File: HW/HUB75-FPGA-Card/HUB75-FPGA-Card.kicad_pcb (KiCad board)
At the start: 4 copper layers, 53.3 x 85.7 mm, 24 parts, among them J1 Conn_02x08_Odd_Even, J2 Conn_02x08_Odd_Even, U1 T20Q100F3, U2 74AHCT245PW, U3 74AHCT245PW, U4 74AHCT245PW, U6 FT232H, U7 93LCxxBxxOT

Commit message: add usb audio implementation
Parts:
- moved U1 14.0 mm to (115.6, 79.4), turned to 45 degrees

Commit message: finish up schematic and begin routing
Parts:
- added C1: 100n, Capacitor_SMD:C_0603_1608Metric, F.Cu at (128.0, 85.3)
- added C10: 1u, Capacitor_SMD:C_0603_1608Metric, F.Cu at (130.6, 90.4)
- added C11: 1u, Capacitor_SMD:C_0603_1608Metric, F.Cu at (124.5, 90.4)
- added C12: 100n, Capacitor_SMD:C_0603_1608Metric, F.Cu at (119.6, 92.2)
- added C13: 4.7u, Capacitor_SMD:C_0603_1608Metric, F.Cu at (121.2, 92.2)
- added C14: 100n, Capacitor_SMD:C_0603_1608Metric, F.Cu at (121.7, 72.9)
- added C15: 100n, Capacitor_SMD:C_0603_1608Metric, F.Cu at (124.7, 78.5)
- added C16: 100n, Capacitor_SMD:C_0603_1608Metric, F.Cu at (124.7, 82.8)
- added C17: 100n, Capacitor_SMD:C_0603_1608Metric, F.Cu at (112.8, 92.2)
- added C18: 100n, Capacitor_SMD:C_0603_1608Metric, F.Cu at (116.6, 92.2)
- added C2: 4.7u, Capacitor_SMD:C_0603_1608Metric, F.Cu at (113.6, 85.6)
- added C20: 100n, Capacitor_SMD:C_0603_1608Metric, F.Cu at (103.9, 81.3)
- added C21: 100n, Capacitor_SMD:C_0603_1608Metric, F.Cu at (103.9, 84.3)
- added C22: 100n, Capacitor_SMD:C_0603_1608Metric, F.Cu at (109.7, 71.6)
- added C23: 1u, Capacitor_SMD:C_0603_1608Metric, F.Cu at (101.4, 77.0)
- added C24: 1u, Capacitor_SMD:C_0603_1608Metric, F.Cu at (101.4, 70.9)
- added C25: 100n, Capacitor_SMD:C_0603_1608Metric, F.Cu at (99.7, 62.9)
- added C26: 100n, Capacitor_SMD:C_0603_1608Metric, F.Cu at (109.9, 62.9)
- added C27: 100n, Capacitor_SMD:C_0603_1608Metric, F.Cu at (120.0, 62.9)
- added C3: 10u, Capacitor_SMD:C_0603_1608Metric, F.Cu at (103.9, 82.8)
- added C36: 100n, Capacitor_SMD:C_0603_1608Metric, F.Cu at (122.9, 141.1)
- added C37: 4.7u, Capacitor_SMD:C_0603_1608Metric, F.Cu at (122.2, 135.5)
- added C38: 100n, Capacitor_SMD:C_0603_1608Metric, F.Cu at (122.2, 138.0)
- added C39: 4.7u, Capacitor_SMD:C_0603_1608Metric, F.Cu at (122.2, 146.2)
- added C4: 1u, Capacitor_SMD:C_0603_1608Metric, F.Cu at (109.2, 93.0)
- added C40: 4.7u, Capacitor_SMD:C_0603_1608Metric, F.Cu at (127.5, 142.3)
- added C41: 100n, Capacitor_SMD:C_0603_1608Metric, F.Cu at (127.5, 144.8)
- added C42: 4.7u, Capacitor_SMD:C_0603_1608Metric, F.Cu at (142.1, 149.3)
- added C43: 100n, Capacitor_SMD:C_0603_1608Metric, F.Cu at (145.0, 149.3)
- added C44: 100n, Capacitor_SMD:C_0603_1608Metric, F.Cu at (147.5, 149.3)
- added C45: 100n, Capacitor_SMD:C_0603_1608Metric, F.Cu at (150.0, 149.3)
- added C46: 100n, Capacitor_SMD:C_0603_1608Metric, F.Cu at (124.2, 152.2)
- added C47: 1u, Capacitor_SMD:C_0603_1608Metric, F.Cu at (118.7, 152.2)
- added C48: 1u, Capacitor_SMD:C_0603_1608Metric, F.Cu at (147.5, 136.6)
- added C49: 1u, Capacitor_SMD:C_0603_1608Metric, F.Cu at (150.0, 136.6)
- added C5: 100n, Capacitor_SMD:C_0603_1608Metric, F.Cu at (118.1, 92.2)
- added C50: 1u, Capacitor_SMD:C_0603_1608Metric, F.Cu at (151.0, 145.7)
- added C51: 1u, Capacitor_SMD:C_0603_1608Metric, F.Cu at (121.7, 99.3)
- added C52: 10u, Capacitor_SMD:C_0603_1608Metric, F.Cu at (120.1, 99.3)
- added C53: 100n, Capacitor_SMD:C_0603_1608Metric, F.Cu at (118.6, 99.3)
- added C54: 100n, Capacitor_SMD:C_0603_1608Metric, F.Cu at (129.3, 99.8)
- added C55: 10u, Capacitor_SMD:C_0603_1608Metric, F.Cu at (107.2, 112.8)
- added C6: 100n, Capacitor_SMD:C_0603_1608Metric, F.Cu at (124.7, 80.5)
- added C7: 100n, Capacitor_SMD:C_0603_1608Metric, F.Cu at (123.2, 72.9)
- added C8: 100n, Capacitor_SMD:C_0603_1608Metric, F.Cu at (117.3, 71.6)
- added C9: 100n, Capacitor_SMD:C_0603_1608Metric, F.Cu at (113.0, 71.6)
- added D1: LED, Diode_SMD:D_0603_1608Metric, F.Cu at (107.5, 148.2)
- added FB3: FerriteBead_Small, Resistor_SMD:R_0603_1608Metric, F.Cu at (102.9, 101.6)
- added FB4: FerriteBead_Small, Resistor_SMD:R_0603_1608Metric, F.Cu at (118.9, 136.3)
- added FB5: FerriteBead_Small, Resistor_SMD:R_0603_1608Metric, F.Cu at (124.2, 143.7)
- added H1: MountingHole, MountingHole:MountingHole_3.2mm_M3, F.Cu at (91.4, 51.4)
- added H2: MountingHole, MountingHole:MountingHole_3.2mm_M3, F.Cu at (91.4, 128.9)
- added H3: MountingHole, MountingHole:MountingHole_3.2mm_M3, F.Cu at (137.2, 51.4)
- added H4: MountingHole, MountingHole:MountingHole_3.2mm_M3, F.Cu at (137.2, 128.9)
- added J1: Conn_02x04_Odd_Even, Connector_PinHeader_2.54mm:PinHeader_2x04_P2.54mm_Vertical, F.Cu at (89.9, 99.8)
- added J10: USB_A_Stacked, Connector_USB:USB_A_CUI_UJ2-ADH-TH_Horizontal_Stacked, F.Cu at (100.9, 114.9)
- added J11: Conn_01x01, Connector_Wire:SolderWire-2sqmm_1x01_D2mm_OD3.9mm, F.Cu at (98.4, 51.4)
- added J12: Conn_01x01, Connector_Wire:SolderWire-2sqmm_1x01_D2mm_OD3.9mm, F.Cu at (130.2, 51.4)
- added J2: Conn_01x03, Connector_PinHeader_2.54mm:PinHeader_1x03_P2.54mm_Vertical, F.Cu at (104.8, 50.8)
- added J4: Conn_01x03, Connector_PinHeader_2.54mm:PinHeader_1x03_P2.54mm_Vertical, F.Cu at (111.1, 50.8)
- added J5: Conn_01x03, Connector_PinHeader_2.54mm:PinHeader_1x03_P2.54mm_Vertical, F.Cu at (117.5, 50.8)
- added J7: Conn_01x03, Connector_PinHeader_2.54mm:PinHeader_1x03_P2.54mm_Vertical, F.Cu at (123.8, 50.8)
- added J8: Conn_01x04, TerminalBlock_Phoenix:TerminalBlock_Phoenix_PT-1,5-4-5.0-H_1x04_P5.00mm_Horizontal, F.Cu at (135.3, 122.4)
- added J9: USB_C_Receptacle_USB2.0, Connector_USB:USB_C_Receptacle_GCT_USB4105-xx-A_16P_TopMnt_Horizontal, F.Cu at (137.2, 97.8)
- added R1: 10k, Resistor_SMD:R_0603_1608Metric, F.Cu at (103.9, 87.4)
- added R10: 10k, Resistor_SMD:R_0603_1608Metric, F.Cu at (110.5, 85.6)
- added R11: 10k, Resistor_SMD:R_0603_1608Metric, F.Cu at (110.5, 87.4)
- added R18: 68R, Resistor_SMD:R_0603_1608Metric, F.Cu at (107.4, 146.5)
- added R19: 10k, Resistor_SMD:R_0603_1608Metric, F.Cu at (108.2, 142.9)
- added R2: 10k, Resistor_SMD:R_0603_1608Metric, F.Cu at (118.6, 81.5)
- added R20: 5.1k, Resistor_SMD:R_0603_1608Metric, F.Cu at (130.8, 102.4)
- added R21: 5.1k, Resistor_SMD:R_0603_1608Metric, F.Cu at (130.8, 93.2)
- added R3: 10k, Resistor_SMD:R_0603_1608Metric, F.Cu at (118.6, 83.3)
- added R4: 10k, Resistor_SMD:R_0603_1608Metric, F.Cu at (118.4, 84.8)
- added R5: 10k, Resistor_SMD:R_0603_1608Metric, F.Cu at (118.6, 86.6)
- added R6: 10k, Resistor_SMD:R_0603_1608Metric, F.Cu at (113.5, 87.4)
- added R7: 10k, Resistor_SMD:R_0603_1608Metric, F.Cu at (103.9, 85.9)
- added R8: 10k, Resistor_SMD:R_0603_1608Metric, F.Cu at (110.5, 84.1)
- added R9: 10k, Resistor_SMD:R_0603_1608Metric, F.Cu at (110.5, 82.5)
- added U10: HS-100B, Package_QFP:LQFP-48_7x7mm_P0.5mm, F.Cu at (115.3, 143.4)
- added U11: PAM8406, Package_SO:SO-16_3.9x9.9mm_P1.27mm, F.Cu at (144.7, 142.5)
- added U12: USBLC6-2SC6, Package_TO_SOT_SMD:SOT-23-6, F.Cu at (128.5, 97.3)
- added U13: CH334R, Package_SO:SSOP-16_3.9x4.9mm_P0.635mm, F.Cu at (122.2, 104.7)
- added U2: XC6206PxxxMR, Package_TO_SOT_SMD:SOT-23-3, F.Cu at (127.5, 90.4)
- added U3: AP2112K-1.2, Package_TO_SOT_SMD:SOT-23-5, F.Cu at (101.4, 73.9)
- added U9: WMM7037AT2, Project:WMM7037AT2, F.Cu at (121.4, 151.6)
- added X1: ECS-2520MV-xxx-xx, Oscillator:Oscillator_SMD_ECS_2520MV-xxx-xx-4Pin_2.5x2.0mm, F.Cu at (125.5, 85.3)
- added Y1: Crystal_GND24, Crystal:Crystal_SMD_3225-4Pin_3.2x2.5mm, F.Cu at (117.6, 103.4)
- C28: renamed from C10; footprint Capacitor_SMD:C_0603_1608Metric_Pad1.08x0.95mm_HandSolder -> Capacitor_SMD:C_0603_1608Metric
- C29: renamed from C11; footprint Capacitor_SMD:C_0603_1608Metric_Pad1.08x0.95mm_HandSolder -> Capacitor_SMD:C_0603_1608Metric
- C30: renamed from C12; footprint Capacitor_SMD:C_0603_1608Metric_Pad1.08x0.95mm_HandSolder -> Capacitor_SMD:C_0603_1608Metric
- C31: renamed from C13; footprint Capacitor_SMD:C_0603_1608Metric_Pad1.08x0.95mm_HandSolder -> Capacitor_SMD:C_0603_1608Metric
- C32: renamed from C14; footprint Capacitor_SMD:C_0603_1608Metric_Pad1.08x0.95mm_HandSolder -> Capacitor_SMD:C_0603_1608Metric
- C33: renamed from C6; footprint Capacitor_SMD:C_0603_1608Metric_Pad1.08x0.95mm_HandSolder -> Capacitor_SMD:C_0603_1608Metric
- C34: renamed from C8; footprint Capacitor_SMD:C_0603_1608Metric_Pad1.08x0.95mm_HandSolder -> Capacitor_SMD:C_0603_1608Metric
- C35: renamed from C5; footprint Capacitor_SMD:C_0603_1608Metric_Pad1.08x0.95mm_HandSolder -> Capacitor_SMD:C_0603_1608Metric
- FB1, FB2: value FerriteBead -> FerriteBead_Small; footprint Resistor_SMD:R_0603_1608Metric_Pad0.98x0.95mm_HandSolder -> Resistor_SMD:R_0603_1608Metric
- R12: renamed from R15; footprint Resistor_SMD:R_0603_1608Metric_Pad0.98x0.95mm_HandSolder -> Resistor_SMD:R_0603_1608Metric
- R13: renamed from R11; footprint Resistor_SMD:R_0603_1608Metric_Pad0.98x0.95mm_HandSolder -> Resistor_SMD:R_0603_1608Metric
- R14: renamed from R12; footprint Resistor_SMD:R_0603_1608Metric_Pad0.98x0.95mm_HandSolder -> Resistor_SMD:R_0603_1608Metric
- R15: renamed from R14; footprint Resistor_SMD:R_0603_1608Metric_Pad0.98x0.95mm_HandSolder -> Resistor_SMD:R_0603_1608Metric
- R16: footprint Resistor_SMD:R_0603_1608Metric_Pad0.98x0.95mm_HandSolder -> Resistor_SMD:R_0603_1608Metric
- R17: renamed from R13; footprint Resistor_SMD:R_0603_1608Metric_Pad0.98x0.95mm_HandSolder -> Resistor_SMD:R_0603_1608Metric
- moved U7 73.5 mm to (99.8, 94.7), turned to 90 degrees
- moved C32 67.9 mm to (93.0, 97.0), turned to 180 degrees
- moved R12 67.7 mm to (98.8, 87.9), turned to 90 degrees
- moved R16 67.0 mm to (98.3, 101.6), turned to -90 degrees
- moved FB2 65.7 mm to (95.2, 101.6), turned to 90 degrees
- moved C34 64.2 mm to (93.0, 91.7), turned to 180 degrees
- moved C33 63.8 mm to (93.0, 93.2), turned to 180 degrees
- moved U8 61.0 mm to (109.2, 102.9)
- moved C28 59.8 mm to (96.8, 101.6), turned to -90 degrees
- moved R17 59.5 mm to (106.2, 102.9), turned to 90 degrees
- moved R15 56.0 mm to (109.7, 105.4), turned to 180 degrees
- moved C31 55.7 mm to (105.4, 90.7)
- moved C29 55.4 mm to (101.3, 101.6), turned to -90 degrees
- moved C30 52.6 mm to (104.6, 99.3)
- moved R13 49.1 mm to (112.0, 101.3), turned to -90 degrees
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- renumbered J1 to J3, J2 to J6, U2 to U4, U3 to U5, U4 to U6, U6 to U7, U7 to U8
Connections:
- C28 pad 1: Net-(U6-VPHY) -> Net-(U7-VPHY)
- C29 pad 1: Net-(U6-VPLL) -> Net-(U7-VPLL)
- FB1 pad 1: +3.3VP -> +1V2
- FB1 pad 2: Net-(U6-VPHY) -> Net-(U1A-VCCA_BR)
- FB2 pad 2: Net-(U6-VPLL) -> Net-(U7-VPHY)
- J3 pad 1: /Hub75/B1 -> /Level Shifters/B1_out
- J3 pad 11: unconnected-(J1-Pin_11-Pad11) -> /Level Shifters/RDAT_out
- J3 pad 13: unconnected-(J1-Pin_13-Pad13) -> /Level Shifters/CLK_out
- J3 pad 14: unconnected-(J1-Pin_14-Pad14) -> /Level Shifters/LAT_out
- J3 pad 15: unconnected-(J1-Pin_15-Pad15) -> /Level Shifters/BLNK_out
- J3 pad 2: /Hub75/G1 -> /Level Shifters/G1_out
- J3 pad 3: /Hub75/R1 -> /Level Shifters/R1_out
- J3 pad 5: /Hub75/B2 -> /Level Shifters/B2_out
- J3 pad 6: /Hub75/G2 -> /Level Shifters/G2_out
- J3 pad 7: /Hub75/R2 -> /Level Shifters/R2_out
- J3 pad 9: unconnected-(J1-Pin_9-Pad9) -> /Level Shifters/RCLK_out
- J6 pad 1: /Hub75/B3 -> /Level Shifters/B3_out
- J6 pad 11: unconnected-(J2-Pin_11-Pad11) -> /Level Shifters/RDAT_out
- J6 pad 13: unconnected-(J2-Pin_13-Pad13) -> /Level Shifters/CLK_out
- J6 pad 14: unconnected-(J2-Pin_14-Pad14) -> /Level Shifters/LAT_out
- J6 pad 15: unconnected-(J2-Pin_15-Pad15) -> /Level Shifters/BLNK_out
- J6 pad 2: /Hub75/G3 -> /Level Shifters/G3_out
- J6 pad 3: /Hub75/R3 -> /Level Shifters/R3_out
- J6 pad 5: /Hub75/B4 -> /Level Shifters/B4_out
- J6 pad 6: /Hub75/G4 -> /Level Shifters/G4_out
- J6 pad 7: /Hub75/R4 -> /Level Shifters/R4_out
- J6 pad 9: unconnected-(J2-Pin_9-Pad9) -> /Level Shifters/RCLK_out
- U1 pad 10: unconnected-(U1B-GPIOL_20_CTRL0_CDI4-Pad10) -> /FPGA/~{TXE}
- U1 pad 100: unconnected-(U1B-GPIOL_46-Pad100) -> /FPGA/B2
- U1 pad 11: unconnected-(U1A-VCCIO1A_1B_1C-Pad11) -> +3V3
- U1 pad 12: unconnected-(U1B-TDO-Pad12) -> /FPGA/TDO
- U1 pad 13: unconnected-(U1B-TCK-Pad13) -> Net-(J1-Pin_3)
- U1 pad 14: unconnected-(U1B-GPIOL_13_CDI3-Pad14) -> /FPGA/CLK_12MHZ
- U1 pad 15: unconnected-(U1A-VCC-Pad15) -> +1V2
- U1 pad 16: unconnected-(U1B-TMS-Pad16) -> /FPGA/TMS
- U1 pad 17: unconnected-(U1B-TDI-Pad17) -> /FPGA/TDI
- U1 pad 2: unconnected-(U1B-GPIOL_41_CDI9-Pad2) -> /FPGA/B1
- U1 pad 20: unconnected-(U1B-CRESET_N-Pad20) -> /FPGA/CRESET_N
- U1 pad 21: unconnected-(U1A-VCCIO1A_1B_1C-Pad21) -> +3V3
- U1 pad 22: unconnected-(U1B-GPIOL_05_CSO-Pad22) -> /FPGA/~{RXF}
- U1 pad 29: unconnected-(U1D-GPIOB_TXP01-Pad29) -> /FPGA/D7
- U1 pad 3: unconnected-(U1B-GPIOL_40_CDI8-Pad3) -> /FPGA/G1
- U1 pad 30: unconnected-(U1D-GPIOB_TXN01-Pad30) -> /FPGA/D6
- U1 pad 31: unconnected-(U1A-VCC-Pad31) -> +1V2
- U1 pad 32: unconnected-(U1D-GPIOB_TXP04-Pad32) -> /FPGA/D5
- U1 pad 33: unconnected-(U1D-GPIOB_TXN04-Pad33) -> /FPGA/D4
- U1 pad 34: unconnected-(U1A-VCCIO4B-Pad34) -> +3V3
- U1 pad 37: unconnected-(U1D-GPIOB_TXP10-Pad37) -> /FPGA/D3
- U1 pad 38: unconnected-(U1D-GPIOB_TXN10-Pad38) -> /FPGA/D2
- U1 pad 4: unconnected-(U1B-GPIOL_32_CTRL4_CDI7-Pad4) -> /FPGA/R1
- U1 pad 40: unconnected-(U1D-GPIOB_RXP00-Pad40) -> /FPGA/D1
- U1 pad 41: unconnected-(U1D-GPIOB_RXN00-Pad41) -> /FPGA/D0
- U1 pad 42: unconnected-(U1A-VCCIO4A-Pad42) -> +3V3
- U1 pad 45: unconnected-(U1A-VCC-Pad45) -> +1V2
- U1 pad 5: unconnected-(U1B-GPIOL_31_CLK7_CDI6-Pad5) -> /FPGA/~{OE}
- U1 pad 50: unconnected-(U1A-VCCA_BR-Pad50) -> Net-(U1A-VCCA_BR)
- U1 pad 54: unconnected-(U1C-GPIOR_157_PLLIN-Pad54) -> Net-(U1C-GPIOR_157_PLLIN)
- U1 pad 60: unconnected-(U1A-VCCIO3D_3E-Pad60) -> +3V3
- U1 pad 64: unconnected-(U1A-VCC-Pad64) -> +1V2
- U1 pad 69: unconnected-(U1A-VCCIO3B_3C-Pad69) -> +3V3
- U1 pad 7: unconnected-(U1B-GPIOL_24_CLK0-Pad7) -> /FPGA/CLK_60MHZ
- U1 pad 72: unconnected-(U1A-VCCA_TR-Pad72) -> Net-(U1A-VCCA_BR)
- U1 pad 73: unconnected-(U1C-GPIOR_88_CDI28-Pad73) -> /FPGA/R3
- U1 pad 74: unconnected-(U1C-GPIOR_87_CDI29-Pad74) -> /FPGA/B3
- U1 pad 75: unconnected-(U1A-VCC-Pad75) -> +1V2
- U1 pad 76: unconnected-(U1A-VCCIO3A-Pad76) -> +3V3
- U1 pad 77: unconnected-(U1C-GPIOR_79_EXTFB1_CDI30-Pad77) -> /FPGA/G3
- U1 pad 78: unconnected-(U1C-GPIOR_78_EXTFB0_CDI31-Pad78) -> /FPGA/G4
- U1 pad 79: unconnected-(U1C-GPIOR_77_PLLIN1-Pad79) -> /FPGA/B4
- U1 pad 8: unconnected-(U1B-GPIOL_12_CDI2-Pad8) -> /FPGA/~{WR}
- U1 pad 80: unconnected-(U1C-GPIOR_76_PLLIN0-Pad80) -> /FPGA/R4
- U1 pad 82: unconnected-(U1A-VCC-Pad82) -> +1V2
- U1 pad 83: unconnected-(U1A-VCC-Pad83) -> +1V2
- U1 pad 84: unconnected-(U1A-VCCA_TL-Pad84) -> Net-(U1A-VCCA_BR)
- U1 pad 85: unconnected-(U1B-GPIOL_75_PLLIN1-Pad85) -> /FPGA/STRIP4
- U1 pad 86: unconnected-(U1B-GPIOL_74_PLLIN0-Pad86) -> /FPGA/STRIP3
- U1 pad 87: unconnected-(U1B-GPIOL_73_EXTFB1_CDI15-Pad87) -> /FPGA/BLANK
- U1 pad 88: unconnected-(U1B-GPIOL_71_NSTATUS-Pad88) -> /FPGA/LAT
- U1 pad 89: unconnected-(U1B-GPIOL_72_EXTFB0_CDI14-Pad89) -> /FPGA/CLKOUT
- U1 pad 9: unconnected-(U1B-GPIOL_21_CTRL1_CDI5-Pad9) -> /FPGA/~{RD}
- U1 pad 91: unconnected-(U1A-VCC-Pad91) -> +1V2
- U1 pad 92: unconnected-(U1B-GPIOL_70_CBSEL0-Pad92) -> /FPGA/ROW_DATA
- U1 pad 93: unconnected-(U1B-GPIOL_69_CBSEL1-Pad93) -> /FPGA/ROW_CLK
- U1 pad 94: unconnected-(U1B-GPIOL_67_CDI13-Pad94) -> /FPGA/STRIP2
- U1 pad 95: unconnected-(U1B-GPIOL_66_CDI12-Pad95) -> /FPGA/STRIP1
- U1 pad 96: unconnected-(U1A-VCCIO1D_1E-Pad96) -> +3V3
- U1 pad 98: unconnected-(U1B-GPIOL_53_CDI10-Pad98) -> /FPGA/R2
- U1 pad 99: unconnected-(U1B-GPIOL_54_CDI11-Pad99) -> /FPGA/G2
- U4 pad 1: unconnected-(U2-A->B-Pad1) -> +5V
- U4 pad 11: unconnected-(U2-B7-Pad11) -> /Level Shifters/LED2_out
- U4 pad 12: unconnected-(U2-B6-Pad12) -> /Level Shifters/LED1_out
- U4 pad 13: unconnected-(U2-B5-Pad13) -> /Level Shifters/R2_out
- U4 pad 14: unconnected-(U2-B4-Pad14) -> /Level Shifters/G2_out
- U4 pad 15: unconnected-(U2-B3-Pad15) -> /Level Shifters/B2_out
- U4 pad 16: unconnected-(U2-B2-Pad16) -> /Level Shifters/B1_out
- U4 pad 17: unconnected-(U2-B1-Pad17) -> /Level Shifters/G1_out
- U4 pad 18: unconnected-(U2-B0-Pad18) -> /Level Shifters/R1_out
- U4 pad 2: unconnected-(U2-A0-Pad2) -> /FPGA/R1
- U4 pad 3: unconnected-(U2-A1-Pad3) -> /FPGA/G1
- U4 pad 4: unconnected-(U2-A2-Pad4) -> /FPGA/B1
- U4 pad 5: unconnected-(U2-A3-Pad5) -> /FPGA/B2
- U4 pad 6: unconnected-(U2-A4-Pad6) -> /FPGA/G2
- U4 pad 7: unconnected-(U2-A5-Pad7) -> /FPGA/R2
- U4 pad 8: unconnected-(U2-A6-Pad8) -> /FPGA/STRIP1
- U4 pad 9: unconnected-(U2-A7-Pad9) -> /FPGA/STRIP2
- U5 pad 1: unconnected-(U3-A->B-Pad1) -> +5V
- U5 pad 14: unconnected-(U3-B4-Pad14) -> /Level Shifters/BLNK_out
- U5 pad 15: unconnected-(U3-B3-Pad15) -> /Level Shifters/LAT_out
- U5 pad 16: unconnected-(U3-B2-Pad16) -> /Level Shifters/CLK_out
- U5 pad 17: unconnected-(U3-B1-Pad17) -> /Level Shifters/RDAT_out
- U5 pad 18: unconnected-(U3-B0-Pad18) -> /Level Shifters/RCLK_out
- U5 pad 2: unconnected-(U3-A0-Pad2) -> /FPGA/ROW_CLK
- U5 pad 3: unconnected-(U3-A1-Pad3) -> /FPGA/ROW_DATA
- U5 pad 4: unconnected-(U3-A2-Pad4) -> /FPGA/CLKOUT
- U5 pad 5: unconnected-(U3-A3-Pad5) -> /FPGA/LAT
- U5 pad 6: unconnected-(U3-A4-Pad6) -> /FPGA/BLANK
- U5 pad 7: unconnected-(U3-A5-Pad7) -> GND
- U5 pad 8: unconnected-(U3-A6-Pad8) -> GND
- U5 pad 9: unconnected-(U3-A7-Pad9) -> GND
- U6 pad 1: unconnected-(U4-A->B-Pad1) -> +5V
- U6 pad 11: unconnected-(U4-B7-Pad11) -> /Level Shifters/R3_out
- U6 pad 12: unconnected-(U4-B6-Pad12) -> /Level Shifters/B3_out
- U6 pad 13: unconnected-(U4-B5-Pad13) -> /Level Shifters/G3_out
- U6 pad 14: unconnected-(U4-B4-Pad14) -> /Level Shifters/G4_out
- U6 pad 15: unconnected-(U4-B3-Pad15) -> /Level Shifters/B4_out
- U6 pad 16: unconnected-(U4-B2-Pad16) -> /Level Shifters/R4_out
- U6 pad 17: unconnected-(U4-B1-Pad17) -> /Level Shifters/LED4_out
- U6 pad 18: unconnected-(U4-B0-Pad18) -> /Level Shifters/LED3_out
- U6 pad 2: unconnected-(U4-A0-Pad2) -> /FPGA/STRIP3
- U6 pad 3: unconnected-(U4-A1-Pad3) -> /FPGA/STRIP4
- U6 pad 4: unconnected-(U4-A2-Pad4) -> /FPGA/R4
- U6 pad 5: unconnected-(U4-A3-Pad5) -> /FPGA/B4
- U6 pad 6: unconnected-(U4-A4-Pad6) -> /FPGA/G4
- U6 pad 7: unconnected-(U4-A5-Pad7) -> /FPGA/G3
- U6 pad 8: unconnected-(U4-A6-Pad8) -> /FPGA/B3
- U6 pad 9: unconnected-(U4-A7-Pad9) -> /FPGA/R3
- U7 pad 1: /FTDI/CLK_12MHZ -> /FPGA/CLK_12MHZ
- U7 pad 13: /FTDI/D0 -> /FPGA/D0
- U7 pad 14: /FTDI/D1 -> /FPGA/D1
- U7 pad 15: /FTDI/D2 -> /FPGA/D2
- U7 pad 16: /FTDI/D3 -> /FPGA/D3
- U7 pad 17: /FTDI/D4 -> /FPGA/D4
- U7 pad 18: /FTDI/D5 -> /FPGA/D5
- U7 pad 19: /FTDI/D6 -> /FPGA/D6
- U7 pad 20: /FTDI/D7 -> /FPGA/D7
- U7 pad 21: /FTDI/~{RXF} -> /FPGA/~{RXF}
- U7 pad 25: /FTDI/~{TXE} -> /FPGA/~{TXE}
- U7 pad 26: /FTDI/~{RD} -> /FPGA/~{RD}
- U7 pad 27: /FTDI/~{WR} -> /FPGA/~{WR}
- U7 pad 29: /FTDI/CLK_60MHZ -> /FPGA/CLK_60MHZ
- U7 pad 3: Net-(U6-VPHY) -> Net-(U7-VPHY)
- U7 pad 30: /FTDI/~{OE} -> /FPGA/~{OE}
- U7 pad 40: /FTDI/VIN -> +5V
- U7 pad 8: Net-(U6-VPLL) -> Net-(U7-VPLL)
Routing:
- net /Level Shifters/BLNK_out: track 0.00 -> 57.6 mm, vias 0 -> 1
- net /Level Shifters/LAT_out: track 0.00 -> 56.9 mm, vias 0 -> 1
- net /Level Shifters/CLK_out: track 0.00 -> 55.0 mm, vias 0 -> 1
- net /Level Shifters/RDAT_out: track 0.00 -> 53.6 mm, vias 0 -> 1
- net /Level Shifters/RCLK_out: track 0.00 -> 50.6 mm, vias 0 -> 1
- net GND: track 0.00 -> 35.8 mm, vias 0 -> 7
- net +3V3: track 0.00 -> 32.4 mm
- net +5V: track 0.00 -> 31.3 mm
- net /FTDI/USB_D+: track 0.00 -> 28.1 mm
- net Net-(U7-EECLK): track 0.00 -> 27.5 mm, vias 0 -> 2
- net /FTDI/USB_D-: track 0.00 -> 27.1 mm
- net Net-(U1A-VCCA_BR): track 0.00 -> 26.6 mm
- net Net-(U7-EECS): track 0.00 -> 25.0 mm, vias 0 -> 2
- net +1V2: track 0.00 -> 24.9 mm
- net /FPGA/CLK_12MHZ: track 0.00 -> 23.3 mm, vias 0 -> 2
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- added copper zone on In2.Cu, net +5V
- added copper zone on In1.Cu, net GND
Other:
- board size 53.3 x 85.7 mm -> 53.3 x 85.1 mm
- board text added: "+L-"
- board text added: "+R-"
- board text added: "5V"
- board text added: "GND"
- board text added: "LED1"
- board text added: "LED2"
- board text added: "LED3"
- board text added: "LED4"
- board text added: "P1"
- board text added: "P2"

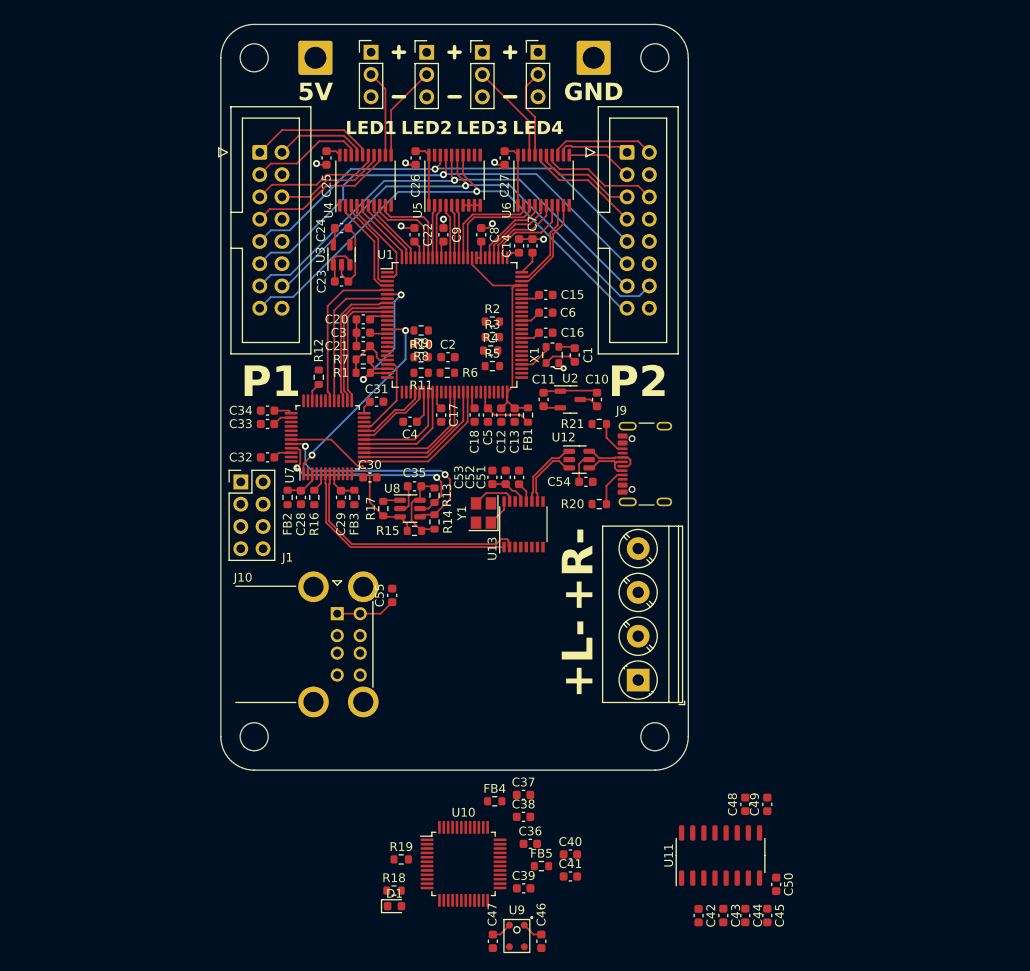
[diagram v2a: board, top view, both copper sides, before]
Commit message: finalize pcb and generate production files for first run
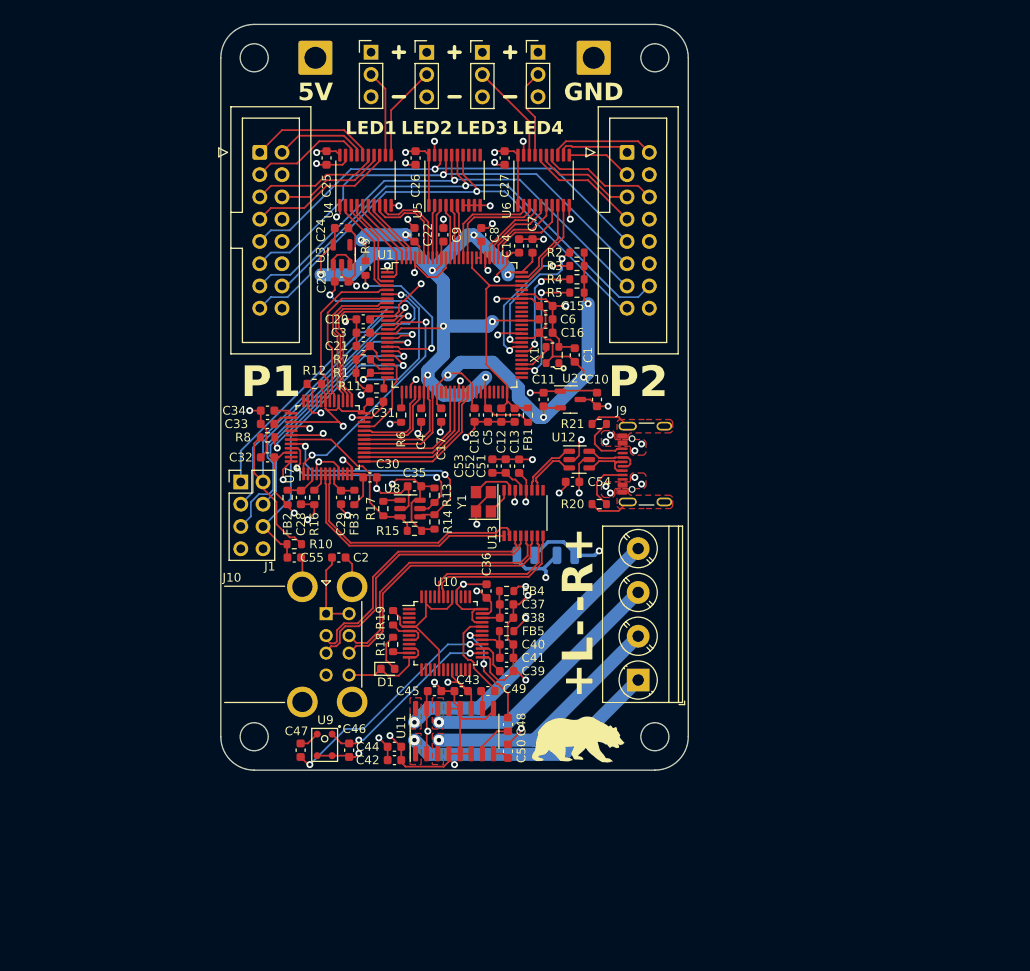
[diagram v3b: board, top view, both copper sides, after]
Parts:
- added G***: LOGO, Project:bear, F.Cu at (128.3, 129.0)
- added J13: Conn_01x01, Connector_Wire:SolderWirePad_1x01_SMD_1x2mm, B.Cu at (128.0, 108.2)
- added J14: Conn_01x01, Connector_Wire:SolderWirePad_1x01_SMD_1x2mm, B.Cu at (126.0, 108.2)
- added J15: Conn_01x01, Connector_Wire:SolderWirePad_1x01_SMD_1x2mm, B.Cu at (123.4, 108.2)
- added J16: Conn_01x01, Connector_Wire:SolderWirePad_1x01_SMD_1x2mm, B.Cu at (121.4, 108.2)
- C42: value 4.7u -> 10u
- C43: value 100n -> 10u
- C48, C49: value 1u -> 10u
- R18: value 68R -> 470R
- moved C45 45.8 mm to (112.0, 123.7), turned to 180 degrees
- moved C44 44.4 mm to (107.4, 130.0), turned to 180 degrees
- moved C43 39.4 mm to (115.1, 123.7), turned to 0 degrees
- moved C42 39.0 mm to (107.4, 131.6), turned to 180 degrees
- moved C49 34.4 mm to (118.1, 123.7), turned to 180 degrees
- moved C50 34.2 mm to (120.4, 130.6), turned to 90 degrees
- moved U11 33.5 mm to (114.3, 128.3)
- moved C46 30.9 mm to (102.3, 130.4)
- moved C47 30.9 mm to (96.7, 130.4)
- moved U9 30.9 mm to (99.5, 129.8)
- moved C36 29.3 mm to (118.0, 112.3), turned to 90 degrees
- moved C2 28.8 mm to (96.0, 108.5)
- moved C48 28.6 mm to (120.4, 127.5), turned to -90 degrees
- moved R18 28.1 mm to (107.3, 118.4), turned to 90 degrees
- moved R19 27.6 mm to (107.3, 115.3), turned to 90 degrees
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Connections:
- net Net-(J1-Pin_3) renamed /FPGA/TCK
- J10 pad 2: /USB Hub/USB3_D- -> /USB Hub/USB4_D-
- J10 pad 3: /USB Hub/USB3_D+ -> /USB Hub/USB4_D+
- J10 pad 6: /USB Hub/USB4_D- -> /USB Hub/USB3_D-
- J10 pad 7: /USB Hub/USB4_D+ -> /USB Hub/USB3_D+
- J8 pad 3: /USB Audio/R+ -> /USB Audio/R-
- J8 pad 4: /USB Audio/R- -> /USB Audio/R+
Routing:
- net GND: track 35.8 -> 231.0 mm, vias 7 -> 48
- net +3V3: track 32.4 -> 212.7 mm, vias 0 -> 12
- net +1V2: track 24.9 -> 100.4 mm, vias 0 -> 8
- net +5V: track 31.3 -> 93.4 mm, vias 0 -> 23
- net +3.3VP: track 14.8 -> 68.4 mm, vias 0 -> 4
- net /FPGA/TMS: track 0.00 -> 36.7 mm, vias 0 -> 1
- net /FPGA/CRESET_N: track 0.00 -> 35.4 mm, vias 0 -> 1
- net /FPGA/TCK: track 0.00 -> 33.9 mm, vias 0 -> 1
- net /USB Audio/R+: track 0.00 -> 33.7 mm, vias 0 -> 1
- net /FPGA/TDO: track 0.00 -> 31.9 mm, vias 0 -> 1
- net /USB Hub/USB4_D+: track 0.00 -> 31.4 mm
- net /USB Hub/USB4_D-: track 0.00 -> 31.0 mm
- net /FPGA/TDI: track 0.00 -> 30.6 mm, vias 0 -> 1
- net /USB Hub/USB3_D+: track 0.00 -> 30.3 mm
- net /USB Audio/L+: track 0.00 -> 29.7 mm, vias 0 -> 1
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- added copper zone on F.Cu, net +5V
- added copper zone on F.Cu, net /USB Audio/L+
- added copper zone on F.Cu, net /USB Audio/L-
- added copper zone on F.Cu, net /USB Audio/R+
- added copper zone on F.Cu, net /USB Audio/R-
- added copper zone on F.Cu, net GND
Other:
- board text added: "-R+"
- board text added: "3V3 TDO TDI TCK TMS RST GND GND"
- board text added: "Aux 5V"
- board text added: "JTAG"
- board text added: "Prototypical Helmet Controller V1.0"
- board text added: "by yocto"
- board text removed: "+R-"

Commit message: beginning of board rev 1.1
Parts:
- R18: value 470R -> 5.1k
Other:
- board text added: "3V3 TDO TDI TCK RST TMS GND GND"
- board text added: "Prototypical Helmet Controller V1.1"
- board text removed: "3V3 TDO TDI TCK TMS RST GND GND"
- board text removed: "Prototypical Helmet Controller V1.0"

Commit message: fix minor pcb annoyances
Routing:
- net +5V: track 93.4 -> 93.7 mm, vias 23 -> 22
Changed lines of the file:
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@@
   (segment (start 126.5683 75.596438) (end 126.5683 74.36852) (width 0.2032) (layer "B.Cu") (net 23))
   (segment (start 113.665 130.845) (end 113.665 131.445) (width 0.2032) (layer "F.Cu") (net 31))
+  (segment (start 112.438 123.347) (end 112.438 123.106) (width 1) (layer "F.Cu") (net 31))
   (segment (start 122.428 115.4895) (end 122.428 115.316) (width 0.2032) (layer "F.Cu") (net 31))
   (segment (start 122.4915 100.778) (end 122.4915 99.6315) (width 0.2032) (layer "F.Cu") (net 31))
   (segment (start 102.266 114.863998) (end 99.646 114.863998) (width 0.2032) (layer "F.Cu") (net 31))
   (segment (start 119.012 62.09) (end 118.872 62.23) (width 0.2032) (layer "F.Cu") (net 31))
+  (segment (start 112.873 123.782) (end 112.789 123.698) (width 1) (layer "F.Cu") (net 31))
   (segment (start 97.79 93.726) (end 97.556 93.492) (width 0.2032) (layer "F.Cu") (net 31))
   (segment (start 117.1675 112.268) (end 117.9545 113.055) (width 0.2032) (layer "F.Cu") (net 31))
   (segment (start 121.0655 116.852) (end 122.428 115.4895) (width 0.2032) (layer "F.Cu") (net 31))
   (segment (start 128.511 97.77) (end 128.999 97.282) (width 0.2032) (layer "F.Cu") (net 31))
+  (segment (start 112.789 123.698) (end 112.438 123.347) (width 1) (layer "F.Cu") (net 31))
   (segment (start 122.4915 99.6315) (end 121.666 98.806) (width 0.2032) (layer "F.Cu") (net 31))
+  (segment (start 114.935 125.695) (end 113.665 125.695) (width 1) (layer "F.Cu") (net 31))
   (segment (start 108.7044 132.3134) (end 113.071599 132.3134) (width 0.2032) (layer "F.Cu") (net 31))
+  (segment (start 113.665 125.669) (end 113.665 125.695) (width 1) (layer "F.Cu") (net 31))
   (segment (start 128.6455 90.424) (end 129.781 90.424) (width 0.2032) (layer "F.Cu") (net 31))
   (segment (start 108.217 130.048) (end 108.217 131.826) (width 0.2032) (layer "F.Cu") (net 31))
-  (segment (start 113.665 125.695) (end 114.935 125.695) (width 0.2032) (layer "F.Cu") (net 31))
   (segment (start 120.015 62.09) (end 119.012 62.09) (width 0.2032) (layer "F.Cu") (net 31))
   (segment (start 128.999 97.282) (end 129.6615 97.282) (width 0.2032) (layer "F.Cu") (net 31))
@@
   (segment (start 113.071599 132.3134) (end 113.665 131.719999) (width 0.2032) (layer "F.Cu") (net 31))
   (segment (start 99.646 114.863998) (end 99.646 109.916684) (width 0.2032) (layer "F.Cu") (net 31))
+  (segment (start 114.203 123.782) (end 112.873 123.782) (width 1) (layer "F.Cu") (net 31))
   (segment (start 111.375 68.2675) (end 111.375 62.5425) (width 0.2032) (layer "F.Cu") (net 31))
-  (segment (start 114.935 125.695) (end 114.935 130.845) (width 0.2032) (layer "F.Cu") (net 31))
-  (segment (start 113.665 131.445) (end 114.3 132.08) (width 0.2032) (layer "F.Cu") (net 31))
+  (segment (start 114.287 123.698) (end 114.203 123.782) (width 1) (layer "F.Cu") (net 31))
   (segment (start 122.4915 100.778) (end 122.4915 102.0445) (width 0.2032) (layer "F.Cu") (net 31))
   (segment (start 108.204 130.048) (end 106.934 128.778) (width 0.2032) (layer "F.Cu") (net 31))
+  (segment (start 115.635001 127.27) (end 118.044999 127.27) (width 1) (layer "F.Cu") (net 31))
+  (segment (start 114.935 126.569999) (end 115.635001 127.27) (width 1) (layer "F.Cu") (net 31))
   (segment (start 121.0825 62.09) (end 121.535 62.5425) (width 0.2032) (layer "F.Cu") (net 31))
   (segment (start 131.813 91.199) (end 131.826 91.186) (width 0.2032) (layer "F.Cu") (net 31))
   (segment (start 116.84 112.268) (end 117.1675 112.268) (width 0.2032) (layer "F.Cu") (net 31))
-  (segment (start 114.935 126.569999) (end 115.236601 126.8716) (width 0.2032) (layer "F.Cu") (net 31))
-  (segment (start 113.665 130.845) (end 114.935 130.845) (width 0.2032) (layer "F.Cu") (net 31))
-  (segment (start 115.236601 126.8716) (end 117.816214 126.8716) (width 0.2032) (layer "F.Cu") (net 31))
   (segment (start 108.217 130.048) (end 108.204 130.048) (width 0.2032) (layer "F.Cu") (net 31))
-  (segment (start 117.816214 126.8716) (end 118.745 125.942814) (width 0.2032) (layer "F.Cu") (net 31))
   (segment (start 129.781 90.424) (end 130.556 91.199) (width 0.2032) (layer "F.Cu") (net 31))
   (segment (start 108.852 62.09) (end 108.712 62.23) (width 0.2032) (layer "F.Cu") (net 31))
   (segment (start 121.5855 111.76) (end 121.0655 112.28) (width 0.2032) (layer "F.Cu") (net 31))
   (segment (start 97.556 93.492) (end 95.6595 93.492) (width 0.2032) (layer "F.Cu") (net 31))
+  (segment (start 112.026 122.694) (end 112.014 122.694) (width 1) (layer "F.Cu") (net 31))
   (segment (start 118.4856 114.577072) (end 118.218672 114.844) (width 0.2032) (layer "F.Cu") (net 31))
   (segment (start 128.511 99.822) (end 128.511 101.079) (width 0.2032) (layer "F.Cu") (net 31))
-  (segment (start 112.789 123.698) (end 114.287 123.698) (width 0.2032) (layer "F.Cu") (net 31))
   (segment (start 128.511 99.822) (end 128.511 97.77) (width 0.2032) (layer "F.Cu") (net 31))
+  (segment (start 114.935 125.695) (end 114.935 126.569999) (width 1) (layer "F.Cu") (net 31))
   (segment (start 113.665 131.719999) (end 113.665 130.845) (width 0.2032) (layer "F.Cu") (net 31))
-  (segment (start 114.935 125.695) (end 114.935 126.569999) (width 0.2032) (layer "F.Cu") (net 31))
   (segment (start 130.556 91.199) (end 131.813 91.199) (width 0.2032) (layer "F.Cu") (net 31))
   (segment (start 122.4915 102.0445) (end 122.428 102.108) (width 0.2032) (layer "F.Cu") (net 31))
+  (segment (start 112.438 123.106) (end 112.026 122.694) (width 1) (layer "F.Cu") (net 31))
   (segment (start 122.428 111.76) (end 121.5855 111.76) (width 0.2032) (layer "F.Cu") (net 31))
   (segment (start 98.724444 62.09) (end 98.568222 62.246222) (width 0.2032) (layer "F.Cu") (net 31))
-  (segment (start 114.287 123.698) (end 114.287 125.047) (width 0.2032) (layer "F.Cu") (net 31))
   (segment (start 121.535 68.2675) (end 121.535 62.5425) (width 0.2032) (layer "F.Cu") (net 31))
   (segment (start 99.695 62.09) (end 100.7625 62.09) (width 0.2032) (layer "F.Cu") (net 31))
@@
   (segment (start 101.215 68.2675) (end 101.215 69.219) (width 0.2032) (layer "F.Cu") (net 31))
   (segment (start 108.217 131.826) (end 108.7044 132.3134) (width 0.2032) (layer "F.Cu") (net 31))
+  (segment (start 118.745 126.569999) (end 118.745 125.695) (width 1) (layer "F.Cu") (net 31))
   (segment (start 117.9545 113.055) (end 118.4856 113.5861) (width 0.2032) (layer "F.Cu") (net 31))
+  (segment (start 114.935 130.845) (end 114.935 125.695) (width 1) (layer "F.Cu") (net 31))
   (segment (start 112.789 123.698) (end 112.789 123.457) (width 0.2032) (layer "F.Cu") (net 31))
+  (segment (start 114.935 130.845) (end 116.205 130.845) (width 1) (layer "F.Cu") (net 31))
+  (segment (start 114.287 123.698) (end 114.287 125.047) (width 1) (layer "F.Cu") (net 31))
   (segment (start 101.215 69.219) (end 100.838 69.596) (width 0.2032) (layer "F.Cu") (net 31))
   (segment (start 118.745 125.942814) (end 118.745 125.695) (width 0.2032) (layer "F.Cu") (net 31))
   (segment (start 109.855 62.09) (end 108.852 62.09) (width 0.2032) (layer "F.Cu") (net 31))
+  (segment (start 113.665 130.845) (end 114.935 130.845) (width 1) (layer "F.Cu") (net 31))
   (segment (start 100.7625 62.09) (end 101.215 62.5425) (width 0.2032) (layer "F.Cu") (net 31))
+  (segment (start 114.287 125.047) (end 113.665 125.669) (width 1) (layer "F.Cu") (net 31))
   (segment (start 99.695 62.09) (end 98.724444 62.09) (width 0.2032) (layer "F.Cu") (net 31))
-  (segment (start 114.935 130.845) (end 116.205 130.845) (width 0.2032) (layer "F.Cu") (net 31))
   (segment (start 100.317 109.245684) (end 100.317 108.458) (width 0.2032) (layer "F.Cu") (net 31))
   (segment (start 118.218672 114.844) (end 117.4465 114.844) (width 0.2032) (layer "F.Cu") (net 31))
-  (segment (start 112.789 123.457) (end 112.014 122.682) (width 0.2032) (layer "F.Cu") (net 31))
+  (segment (start 118.044999 127.27) (end 118.745 126.569999) (width 1) (layer "F.Cu") (net 31))
   (segment (start 109.855 62.09) (end 110.9225 62.09) (width 0.2032) (layer "F.Cu") (net 31))
-  (segment (start 114.287 125.047) (end 114.935 125.695) (width 0.2032) (layer "F.Cu") (net 31))
   (via (at 118.872 62.23) (size 0.8) (drill 0.4) (layers "F.Cu" "B.Cu") (net 31))
   (via (at 130.81 107.696) (size 0.8) (drill 0.4) (layers "F.Cu" "B.Cu") (net 31))
@@
   (via (at 98.568222 62.246222) (size 0.8) (drill 0.4) (layers "F.Cu" "B.Cu") (net 31))
   (via (at 135.636 100.076) (size 0.8) (drill 0.4) (layers "F.Cu" "B.Cu") (free) (net 31))
-  (via (at 114.3 132.08) (size 0.8) (drill 0.4) (layers "F.Cu" "B.Cu") (net 31))
   (via (at 116.84 112.268) (size 0.8) (drill 0.4) (layers "F.Cu" "B.Cu") (net 31))
   (via (at 128.524 101.092) (size 0.8) (drill 0.4) (layers "F.Cu" "B.Cu") (net 31))
